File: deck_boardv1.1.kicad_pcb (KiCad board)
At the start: 2 copper layers, 146.7 x 69.5 mm, 60 parts, among them J1 D-Sub 15 Pin Female Socket, Q1 Q_PMOS_GSD, Q2 Q_PMOS_GSD, Q3 NMOS, Q4 Q_PI, Q5 TIP122, Q6 Q_NPN_BEC, SW1 SAFE_switch, SW3 SAFE_switch, U1 Raspberry Pi Zero 2 W, U2 LT8610AC, U3 XBP24-Z7SIT-004, U4 ADP7158ARDZ-3.3-R7

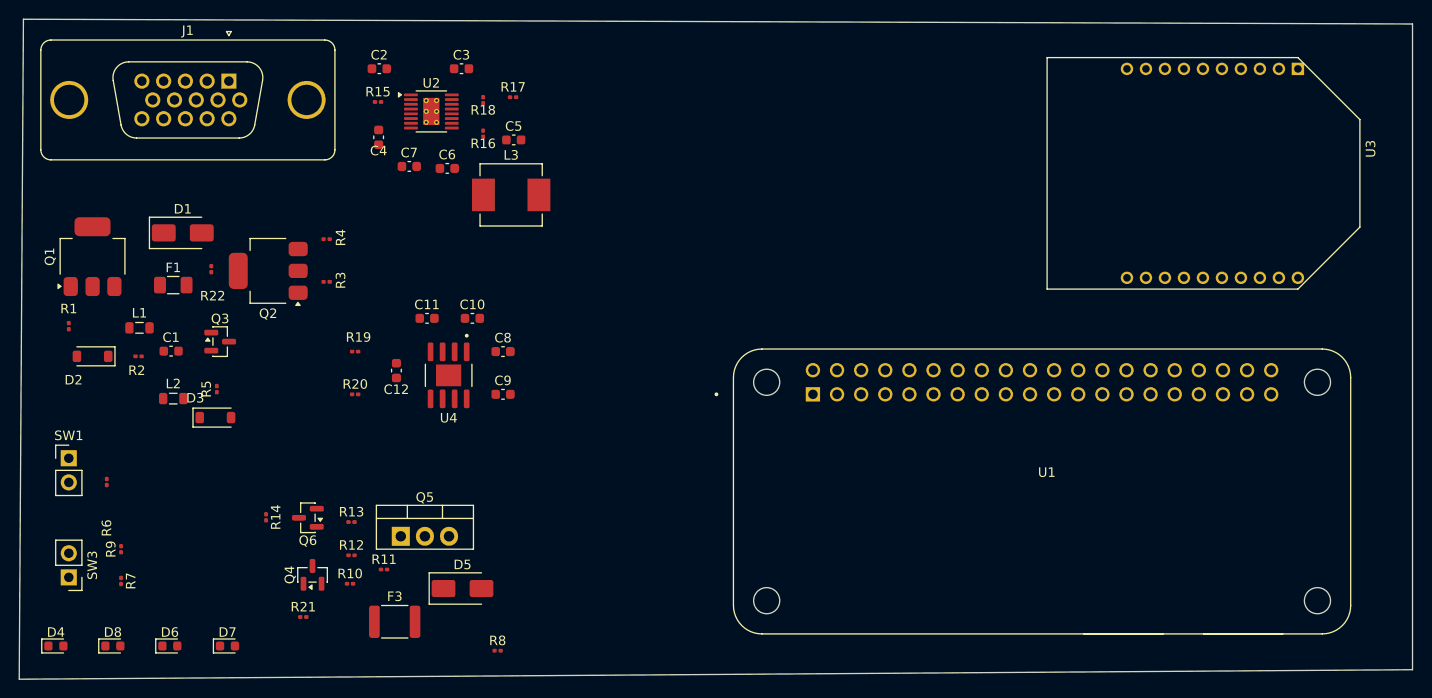
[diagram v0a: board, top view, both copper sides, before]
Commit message: Adjusted PCB so that D-sub and burn-element are off the board.
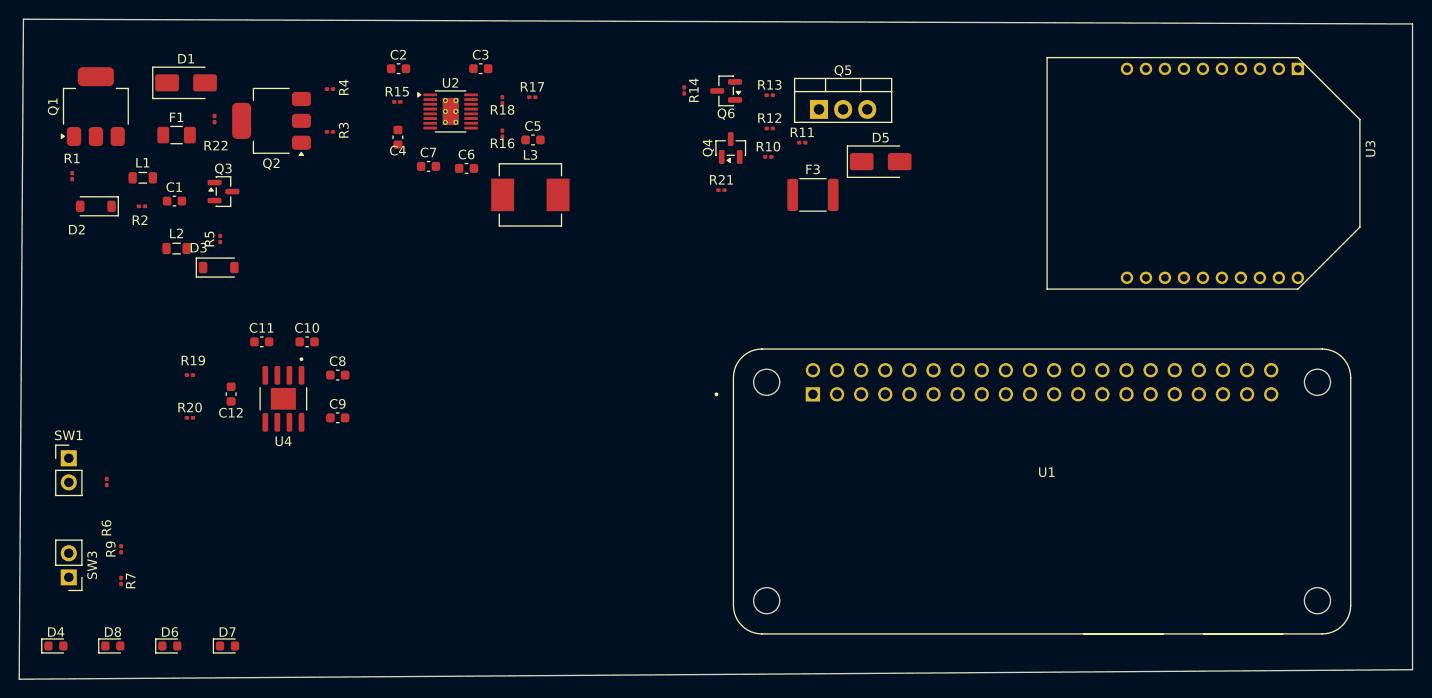
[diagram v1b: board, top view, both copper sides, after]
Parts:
- removed J1: D-Sub 15 Pin Female Socket, Connector_Dsub:DSUB-15-HD_Socket_Vertical_P2.29x1.98mm_MountingHoles
- removed R8: R, Resistor_SMD:R_0201_0603Metric
- moved R11 62.9 mm to (137.7, 68.0)
- moved D5 62.9 mm to (146.0, 70.0)
- moved F3 62.9 mm to (138.9, 73.5)
- moved Q4 62.9 mm to (130.2, 68.6)
- moved Q5 62.9 mm to (139.5, 64.5)
- moved Q6 62.9 mm to (129.7, 62.5)
- moved R10 62.9 mm to (134.2, 69.5)
- moved R12 62.9 mm to (134.3, 66.5)
- moved R13 62.9 mm to (134.3, 63.0)
- moved R14 62.9 mm to (125.3, 62.5)
- moved R21 62.9 mm to (129.2, 73.0)
- moved C10 17.6 mm to (85.6, 89.0)
- moved C11 17.6 mm to (80.8, 89.0)
- moved C12 17.6 mm to (77.6, 94.5)
- moved C8 17.6 mm to (88.8, 92.5)
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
